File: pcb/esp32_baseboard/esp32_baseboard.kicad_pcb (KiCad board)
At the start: 4 copper layers, 180 x 120 mm, 95 parts, among them J1 24V IN, J14 COUNT, J15 FIBER, U1 STM32G030, U2 MP1584EN, U3 TMC1, U4 TMC2, U44 PC817, U45 PC817, U46 PC817, U47 PC817, U5 CH340C, U6 AMS1117-3.3, Y1 12MHz

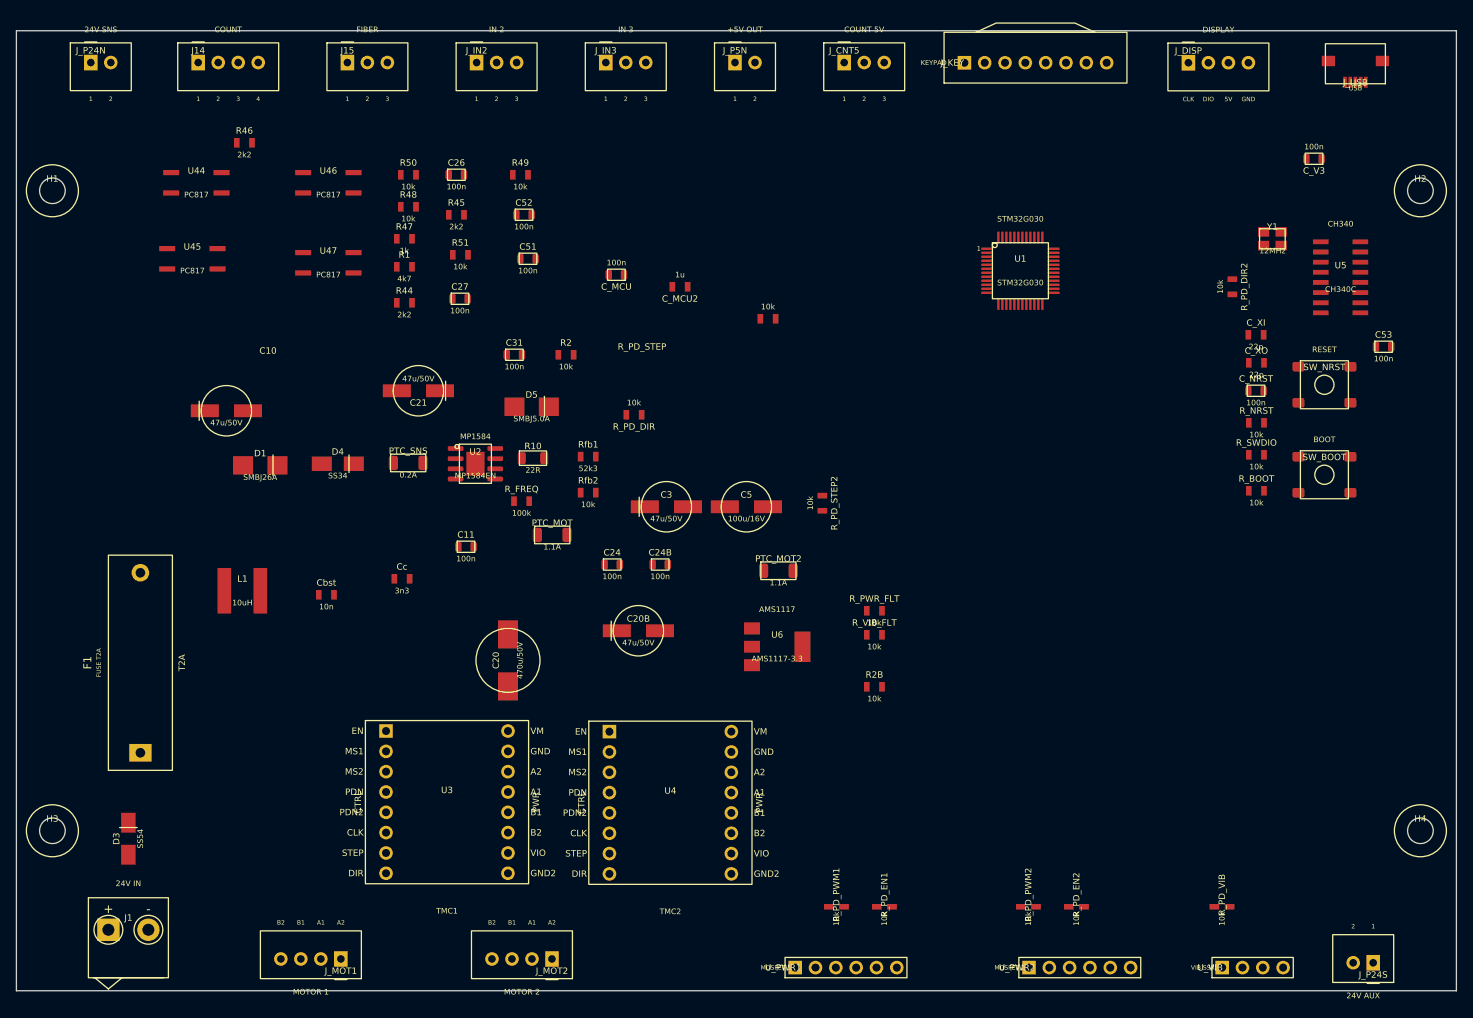
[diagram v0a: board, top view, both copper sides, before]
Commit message: thu nhỏ board và đi dây bằng tay cho stm32
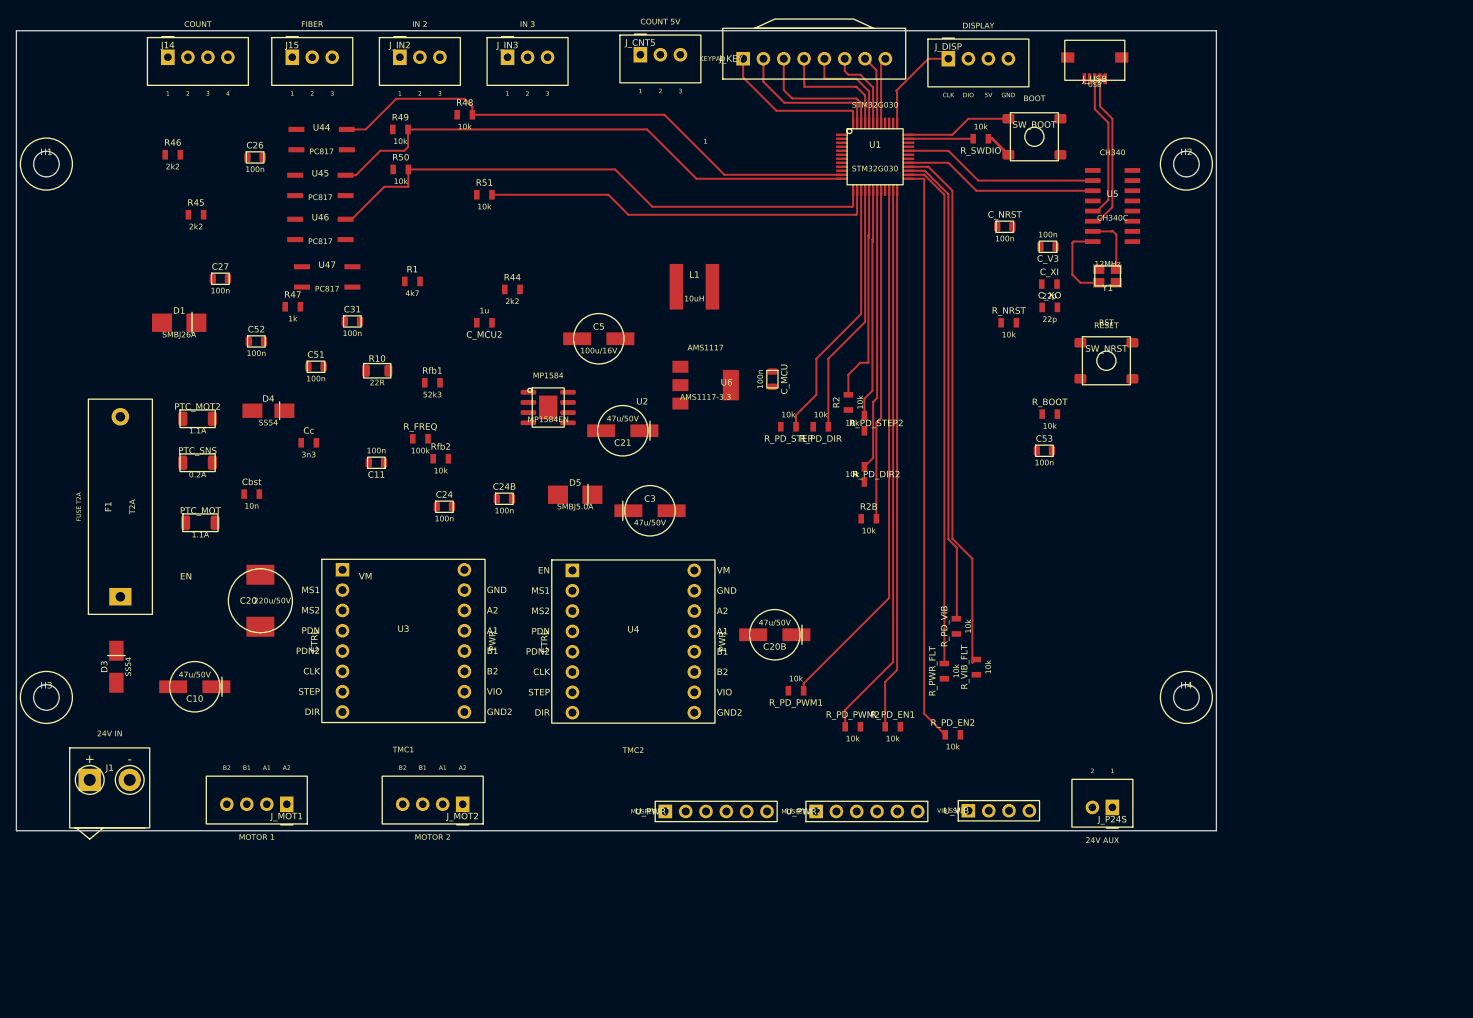
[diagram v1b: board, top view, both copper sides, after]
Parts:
- removed J_P24N: 24V SNS, ESP32_Carrier:JST_XH_02_Socket
- removed J_P5N: +5V OUT, ESP32_Carrier:JST_XH_02_Socket
- C20: value 470u/50V -> 220u/50V
- D4: value SS34 -> SS54
- moved PTC_MOT2 75.0 mm to (72.7, 98.5)
- moved L1 68.1 mm to (134.8, 82.0)
- moved SW_BOOT 55.7 mm to (177.2, 63.2)
- moved R_SWDIO 52.4 mm to (170.6, 63.5), turned to 180 degrees
- moved R_PD_DIR2 51.6 mm to (156.0, 105.5)
- moved R_PD_VIB 48.3 mm to (167.5, 124.5), turned to 90 degrees
- moved C53 44.3 mm to (178.5, 102.5)
- moved PTC_MOT 44.0 mm to (73.0, 111.5)
- moved J_P24S 37.9 mm to (187.0, 147.1)
- moved C_NRST 37.5 mm to (173.6, 74.5)
- moved U_VIB 37.3 mm to (169.0, 147.5)
- moved C52 37.0 mm to (80.0, 88.8)
- moved R2 35.8 mm to (154.0, 96.5), turned to 90 degrees
- moved C_V3 35.0 mm to (178.9, 77.0)
- moved C10 34.7 mm to (72.3, 132.0), turned to 180 degrees
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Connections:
- J14 pad 4: unconnected-(J14-ENC_B-Pad4) -> +24V_SNS
- U1 pad 11: /STEP -> /BUP
- U1 pad 12: /DIR -> /IN2
- U1 pad 13: /EN_TMC -> /IN3
- U1 pad 14: /BUP -> /CNT5
- U1 pad 15: /TM_CLK -> /STEP
- U1 pad 16: /TM_DIO -> /DIR
- U1 pad 17: /STEP2 -> /EN_TMC
- U1 pad 18: /DIR2 -> /STEP2
- U1 pad 19: /KEY_R0 -> /DIR2
- U1 pad 20: /KEY_R1 -> /EN_TMC2
- U1 pad 21: /KEY_R2 -> unconnected-(U1-21-Pad21)
- U1 pad 22: /KEY_R3 -> /PWM_OUT1
- U1 pad 23: /KEY_C0 -> /PWM_OUT2
- U1 pad 24: /KEY_C1 -> /PWR_EN1
- U1 pad 25: /KEY_C2 -> /PWR_EN2
- U1 pad 26: /KEY_C3 -> /PWR_FAULT
- U1 pad 27: /IN2 -> /VIB_CTRL
- U1 pad 28: /EN_TMC2 -> /VIB_FAULT
- U1 pad 33: /PWM_OUT1 -> unconnected-(U1-33-Pad33)
- U1 pad 34: /PWM_OUT2 -> unconnected-(U1-34-Pad34)
- U1 pad 37: unconnected-(U1-P37-Pad37) -> /TM_CLK
- U1 pad 38: unconnected-(U1-P38-Pad38) -> /TM_DIO
- U1 pad 39: /CNT5 -> unconnected-(U1-39-Pad39)
- U1 pad 41: unconnected-(U1-P41-Pad41) -> /KEY_C3
- U1 pad 42: unconnected-(U1-P42-Pad42) -> /KEY_C2
- U1 pad 43: /IN3 -> /KEY_C1
- U1 pad 44: /PWR_EN1 -> /KEY_C0
- U1 pad 45: /PWR_EN2 -> /KEY_R3
- U1 pad 46: /PWR_FAULT -> /KEY_R2
- U1 pad 47: /VIB_CTRL -> /KEY_R1
- U1 pad 48: /VIB_FAULT -> /KEY_R0
- U2 pad 2: (no net) -> unconnected-(U2-2-Pad2)
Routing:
- net /PWR_EN2: track 0.00 -> 72.5 mm
- net /IN3: track 0.00 -> 71.3 mm
- net /PWM_OUT2: track 0.00 -> 69.6 mm
- net /IN2: track 0.00 -> 68.3 mm
- net /BUP: track 0.00 -> 68.0 mm
- net /PWR_EN1: track 0.00 -> 67.7 mm
- net /VIB_FAULT: track 0.00 -> 67.4 mm
- net /PWM_OUT1: track 0.00 -> 67.0 mm
- net /PWR_FAULT: track 0.00 -> 64.1 mm
- net /VIB_CTRL: track 0.00 -> 59.7 mm
- net /CNT5: track 0.00 -> 49.7 mm
- net /EN_TMC2: track 0.00 -> 41.3 mm
- net /DIR2: track 0.00 -> 35.2 mm
- net /STEP: track 0.00 -> 33.0 mm
- net /DIR: track 0.00 -> 31.5 mm
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- removed copper zone on In2.Cu, net +24V
- removed copper zone on In2.Cu, net +3V3
- removed copper zone on In2.Cu, net +5V
- removed copper zone on In1.Cu, net GND
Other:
- board size 180 x 120 mm -> 150 x 100 mm
- copper layers 4 -> 2
- board text added: "150x100 | L/R 8mm DIN/clip | box 180x130 / 200x150"
- board text removed: "180x120 | L/R 8mm DIN/clip | box 180x130 / 200x150"

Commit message: đi dây bằng tay hoàn thiện cho board. không dùng LLM AI
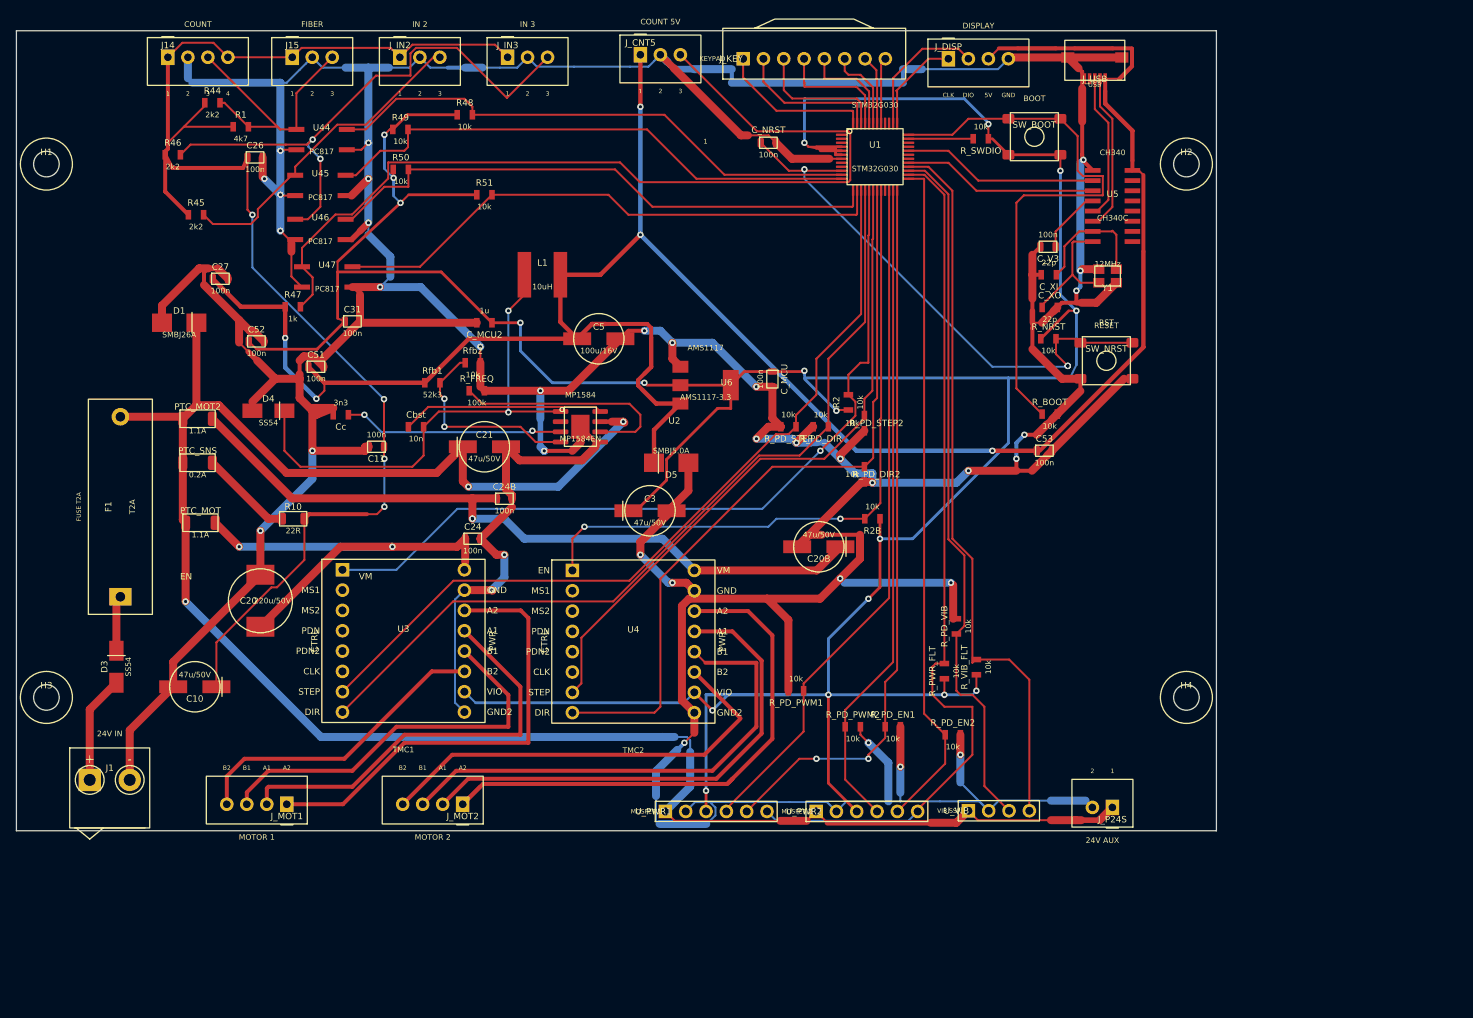
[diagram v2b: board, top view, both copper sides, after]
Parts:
- moved R44 44.2 mm to (74.5, 59.0)
- moved C_NRST 31.4 mm to (144.0, 64.0)
- moved R1 28.9 mm to (78.0, 62.0)
- moved Cbst 22.2 mm to (100.0, 99.5)
- moved R10 21.3 mm to (84.6, 111.0)
- moved L1 19.1 mm to (115.8, 80.5)
- moved C21 17.4 mm to (108.5, 102.0), turned to 0 degrees
- moved D5 12.6 mm to (131.8, 104.0), turned to 180 degrees
- moved Rfb2 12.6 mm to (107.0, 91.5)
- moved C20B 12.3 mm to (150.3, 114.5)
- moved R_FREQ 9.26 mm to (107.5, 95.0)
- moved C24 5.35 mm to (107.0, 113.5)
- moved R_NRST 5.34 mm to (179.0, 88.5)
- moved Cc 5.32 mm to (90.5, 98.0), turned to 180 degrees
- moved U2 4.69 mm to (120.5, 99.5)
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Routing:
- net GND: track 0.00 -> 914.7 mm, vias 0 -> 37
- net +3V3: track 3.33 -> 453.8 mm, vias 0 -> 18
- net +5V: track 0.00 -> 279.8 mm, vias 0 -> 5
- net +24V: track 0.00 -> 252.7 mm, vias 0 -> 3
- net +24V_SNS: track 0.00 -> 180.5 mm, vias 0 -> 4
- net /OPTO_IN_5V: track 0.00 -> 115.0 mm
- net +24V_MOT2: track 0.00 -> 92.1 mm, vias 0 -> 2
- net /DIR: track 31.5 -> 107.0 mm
- net /EN_TMC: track 27.7 -> 102.3 mm, vias 0 -> 1
- net /OPTO_IN3: track 0.00 -> 70.9 mm, vias 0 -> 2
- net /STEP: track 33.0 -> 103.4 mm
- net /Mot2A2: track 0.00 -> 69.8 mm
- net /NRST: track 0.00 -> 69.6 mm, vias 0 -> 3
- net /BUCK_SW: track 0.00 -> 63.6 mm, vias 0 -> 2
- net /Mot2A1: track 0.00 -> 62.6 mm
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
